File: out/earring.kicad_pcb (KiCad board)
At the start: 4 copper layers, 30.5 x 35.8 mm, 138 parts, among them J1 USB-C, Q1 ALS-PT19, Q2 CJ2101, Q3 BSS138W, SW1 BOOTSEL, SW2 PWR, U1 RP2350A, U2 LGS4056H, U3 NCP730-3.3, U4 TPS22913, U5 USBLC6-2P6, U6 LSM6DS3TR-C, U7 W25Q16JVUXIQ, Y1 12MHz

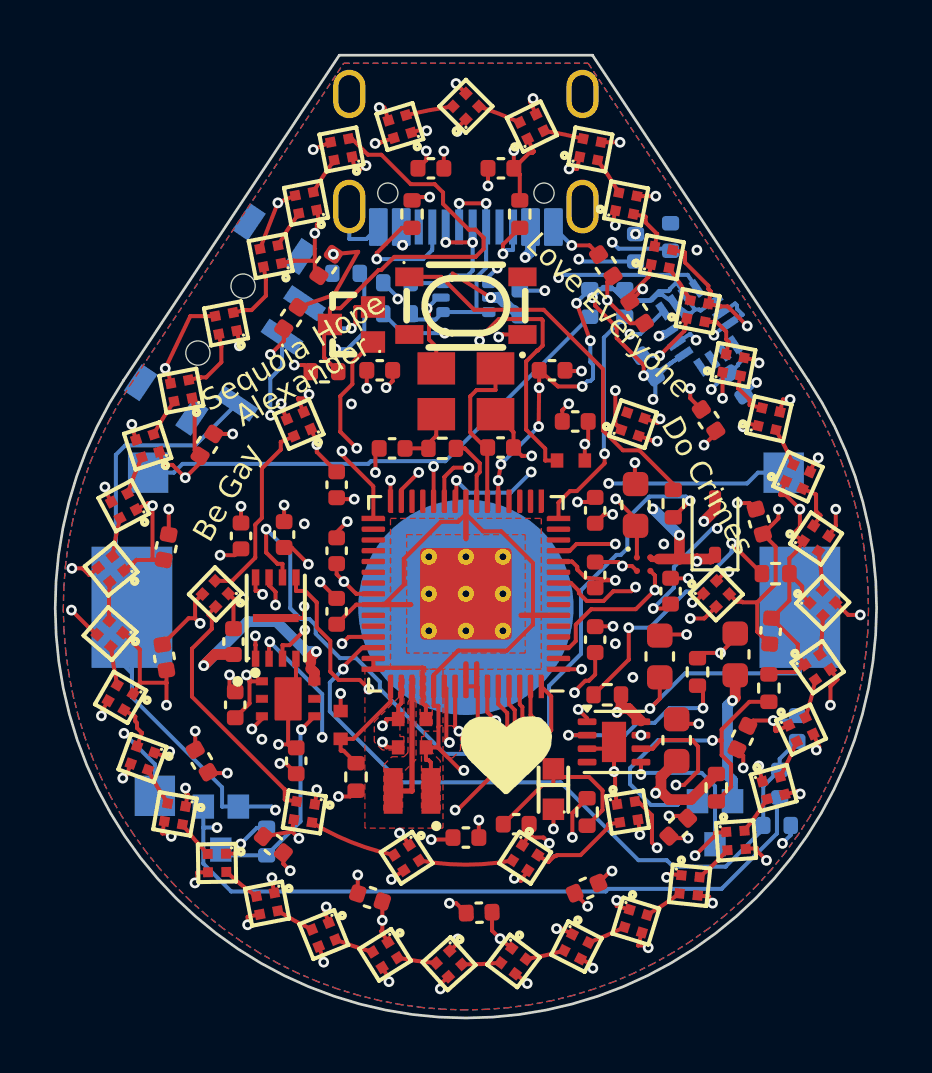
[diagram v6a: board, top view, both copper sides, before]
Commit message: LiPo power source: LPR302823 on wire pads, B3U soft-latch power button
Replaces the RJD2032C1 coin cell + MY-2032-12-R clip with a LiPol
LPR302823 round pouch (Ø28 D-cut, 140 mAh) taped to the back and wired to
two pre-tinned pads beside J1. Placed and DRC-clean (0 errors), NOT routed:
routing is deferred to a new autorouter.

- BT1 -> BAT_LPR302823_PADS (no LCSC part). Pads sit >=0.6 mm from all
  other copper, and route.py keeps vias >=0.6 mm off them.
- R8 22k -> 18k (50 mA; cell max 70 mA). CV stays 4.20 V because the cell's
  PCM can trip as low as 4.305 V.
- SW2 slide switch -> Omron B3U-3000P side-push on the left tip edge, plus
  a CPU-held soft latch (Q4 CJ2101, Q5 BSS138W, D4 BAV70W, R24/R25, C27;
  GPIO20 PWR_HOLD, GPIO21 BTN_SENSE). The Ø28 cell covers the old switch
  spot at every legal angle. Firmware must now hold PWR_HOLD.
- route.py: the coin clip's via keepouts are gone (back centre now
  routable), and a polygon-accurate fallback is added for the tip-LED VLED
  via search.
- design/: intent, brief, decisions and gate evidence for phases 0/1/2/4/6,
  each with an independent review. Datasheets are in design/datasheets/.

The coin-cell rev 2 is commit 4538da2.

Co-Authored-By: Claude Opus 5.5 <noreply@anthropic.com>
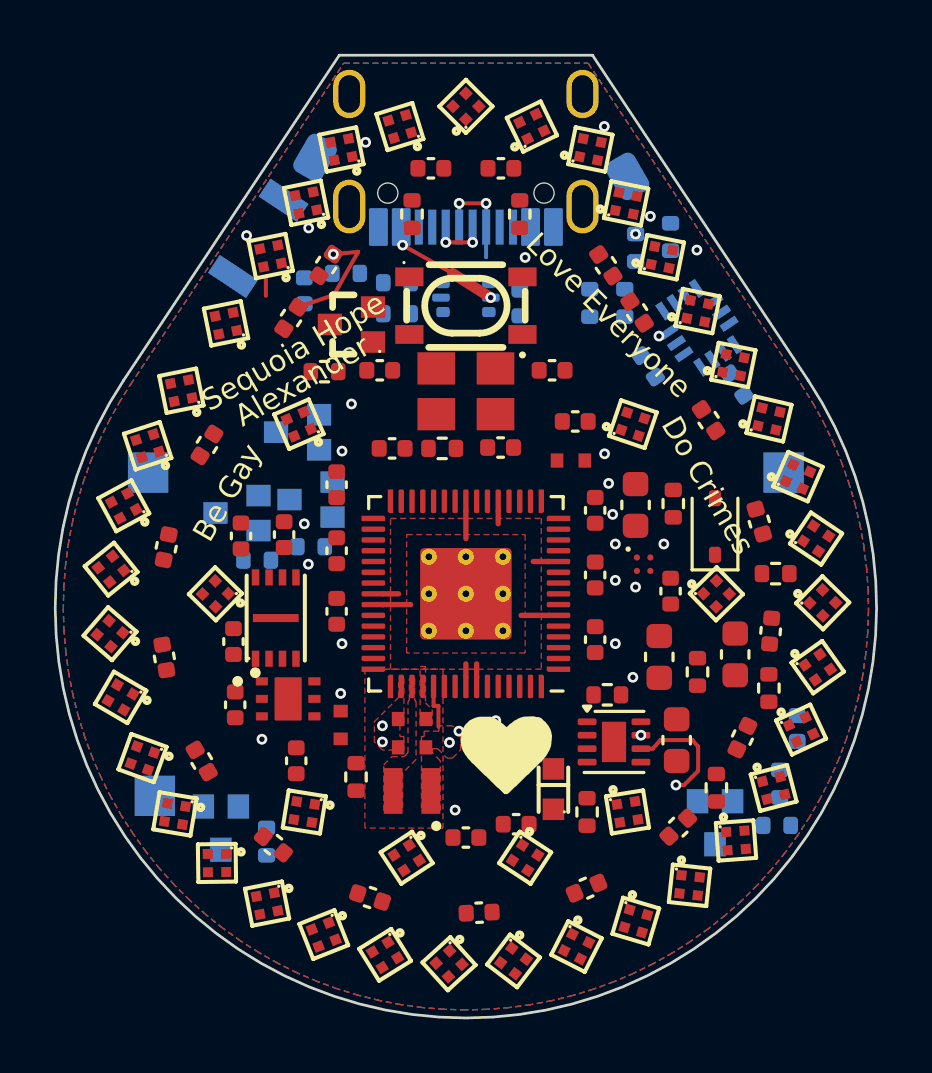
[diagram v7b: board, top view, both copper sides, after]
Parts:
- added C27: 100n, earring:C_0402_1005Metric, B.Cu at (94.0, 88.2)
- added D4: BAV70W, earring:SOT-323_BAT54SW, B.Cu at (93.8, 93.5)
- added Q4: CJ2101, earring:SOT-323_MOSFET, B.Cu at (91.5, 96.5)
- added Q5: BSS138W, earring:SOT-323_MOSFET, B.Cu at (94.2, 96.0)
- added R24: 100k, earring:R_0402_1005Metric, B.Cu at (92.2, 98.2)
- added R25: 100k, earring:R_0402_1005Metric, B.Cu at (94.2, 97.8)
- BT1: value MY-2032-12-R -> LPR302823; footprint earring:BAT_MY2032_12R -> earring:BAT_LPR302823_PADS
- R8: value 22k -> 18k
- SW2: footprint earring:SW-TH_MSK12C02 -> earring:SW_B3U-3000P
- moved SW2 3.46 mm to (92.3, 86.3), turned to -123.6 degrees
- turned LED33 to 168.563 degrees
- turned LED7 to -61.5215 degrees
- turned C34 to -122.093 degrees
- turned LED31 to 168.563 degrees
- turned LED18 to 52.6709 degrees
- turned LED21 to 83.8143 degrees
- turned LED2 to -78.5634 degrees
- turned C56 to 106.292 degrees
- turned LED29 to 166.863 degrees
- turned LED24 to 114.958 degrees
- turned C32 to -123.563 degrees
- turned LED3 to -78.5634 degrees
- turned LED26 to 135.72 degrees
- turned C40 to -59.8064 degrees
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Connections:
- SW2 pad 1: VBATT -> GND
- SW2 pad 2: SW_ON -> BTN_N
- U1 pad 32: (no net) -> PWR_HOLD
- U1 pad 33: (no net) -> BTN_SENSE
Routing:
- net GND: track 135.3 -> 0.00 mm, vias 83 -> 3
- net VLED: track 83.6 -> 4.17 mm, vias 63 -> 7
- net 3V3: track 64.6 -> 2.69 mm, vias 30 -> 8
- net VBATT: track 56.9 -> 0.00 mm, vias 3 -> 0
- net VDD_CORE: track 59.3 -> 4.46 mm, vias 3 -> 0
- net VBUS: track 52.6 -> 3.81 mm, vias 6 -> 3
- net SW_ON: track 46.1 -> 0.00 mm, vias 2 -> 0
- net VSYS: track 38.2 -> 0.00 mm, vias 6 -> 0
- net BOOTSEL: track 30.9 -> 0.00 mm, vias 3 -> 0
- net CHRG: track 26.5 -> 0.00 mm
- net VBSENSE: track 26.1 -> 0.00 mm, vias 1 -> 0
- net PWR_EN: track 25.9 -> 0.00 mm, vias 2 -> 0
- net SWDIO: track 22.7 -> 0.00 mm, vias 3 -> 1
- net LED_EN: track 22.2 -> 0.00 mm, vias 3 -> 1
- net RUN: track 20.3 -> 0.00 mm, vias 1 -> 0
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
